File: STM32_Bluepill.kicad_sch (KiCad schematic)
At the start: 18 parts

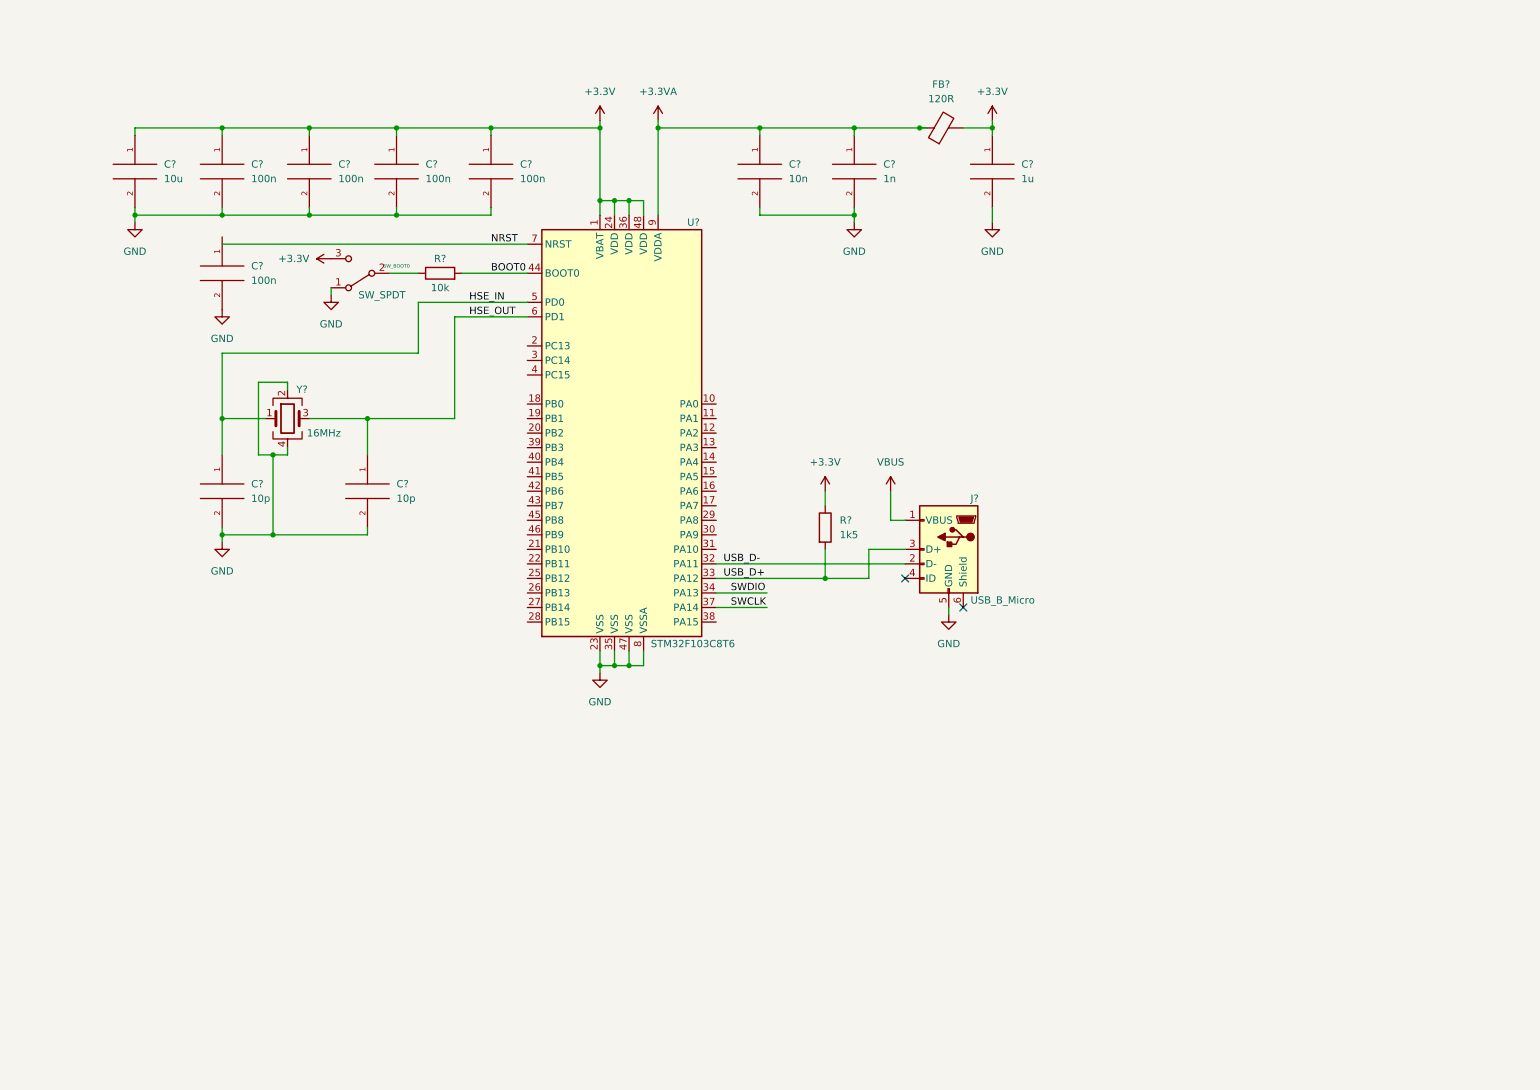
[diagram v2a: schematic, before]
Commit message: Schematic: Add power supply and connectors
	- 3.3V Linear regulator with PWR_LED
	- Connectors for USART and I2C
	- Many resistors are 1.5k to save on the BOM
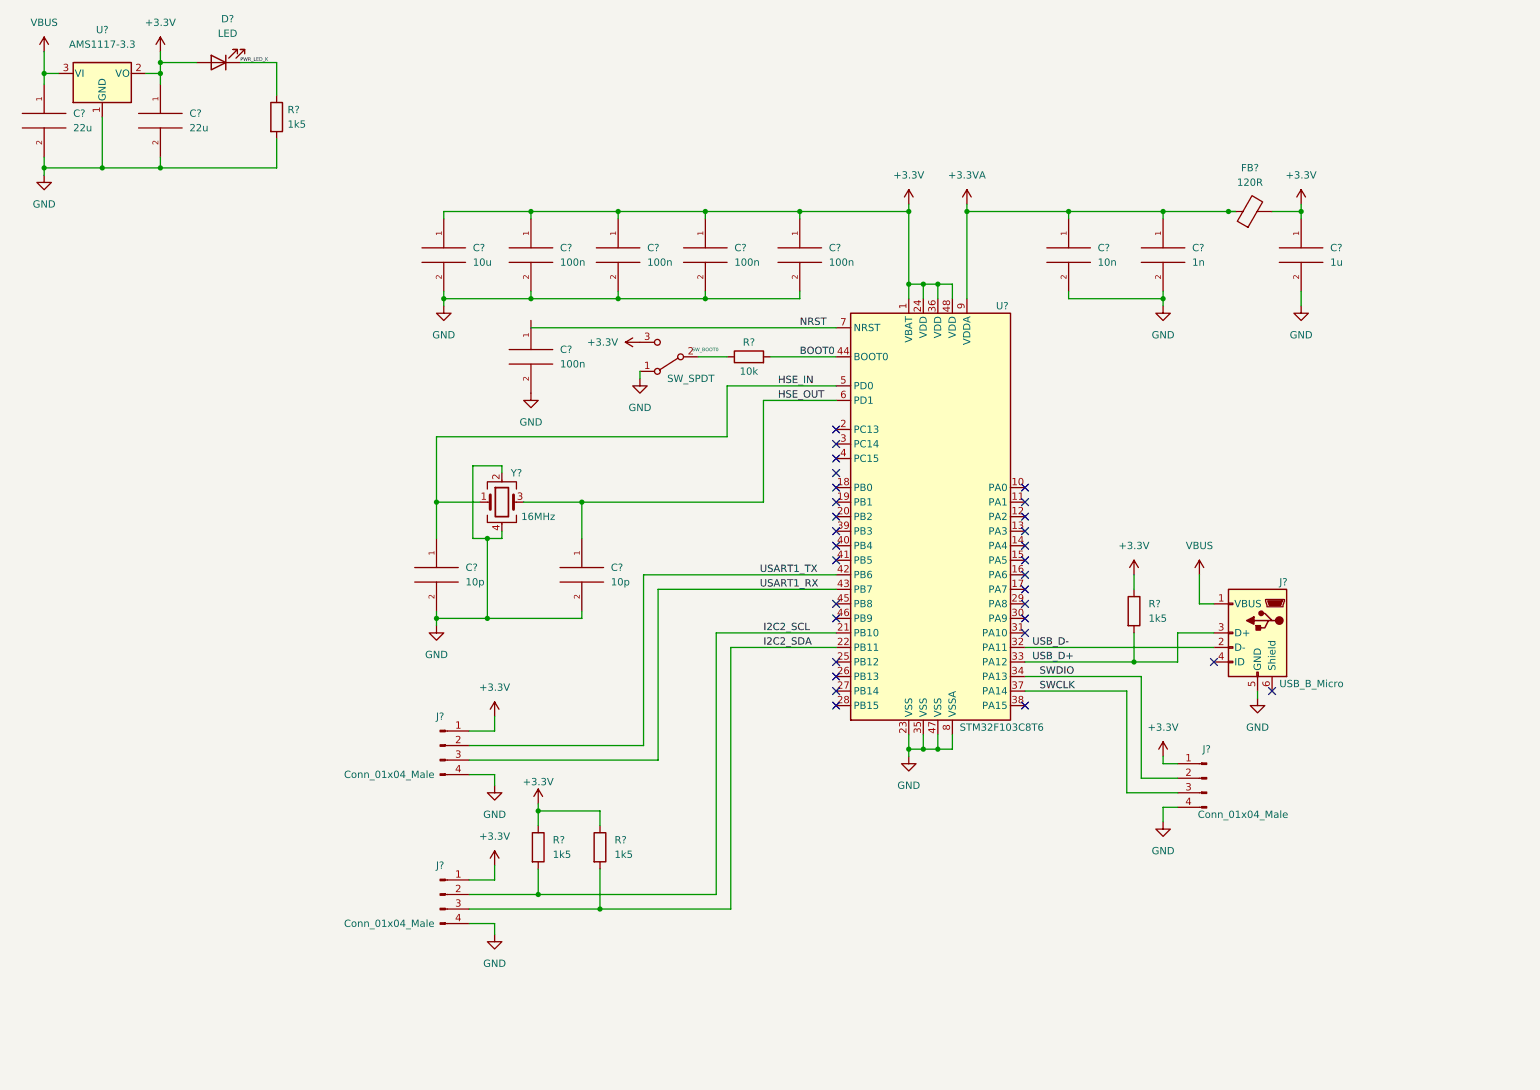
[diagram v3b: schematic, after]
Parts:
- added C? (x2): 22u, symbol pspice:C
- added D?: LED, symbol Device:LED
- added J? (x3): Conn_01x04_Male, symbol Connector:Conn_01x04_Male
- added R? (x3): 1k5, symbol Device:R
- added U?: AMS1117-3.3, Package_TO_SOT_SMD:SOT-223-3_TabPin2, symbol Regulator_Linear:AMS1117-3.3
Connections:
- net +3.3V: now also C?.1, D?.2 (A), J?.1 (Pin_1), J?.1 (Pin_1), J?.1 (Pin_1), R?.1, R?.1, U?.2 (VO)
- net GND: now also C?.2, C?.2, J?.4 (Pin_4), J?.4 (Pin_4), J?.4 (Pin_4), R?.2, U?.1 (GND)
- net SWCLK: now also J?.3 (Pin_3)
- net SWDIO: now also J?.2 (Pin_2)
- net VBUS: now also C?.1, U?.3 (VI)
- net I2C2_SCL: now reaches U?.21 (PB10)
- net I2C2_SCL: now also J?.2 (Pin_2), R?.2
- net I2C2_SDA: now reaches U?.22 (PB11)
- net I2C2_SDA: now also J?.3 (Pin_3), R?.2
- net USART1_TX: now reaches U?.42 (PB6)
- net USART1_TX: now also J?.2 (Pin_2)
- net USART1_RX: now reaches U?.43 (PB7)
- net USART1_RX: now also J?.3 (Pin_3)
- new net PWR_LED_K: D?.1 (K), R?.1
- no-connect marks 2 -> 30
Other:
- moved on the sheet: C?, FB?, J?, R?, SW_BOOT0, U?, Y?

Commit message: Schematic: Annotate and add notes and run ERC; also add PWR_FLAG
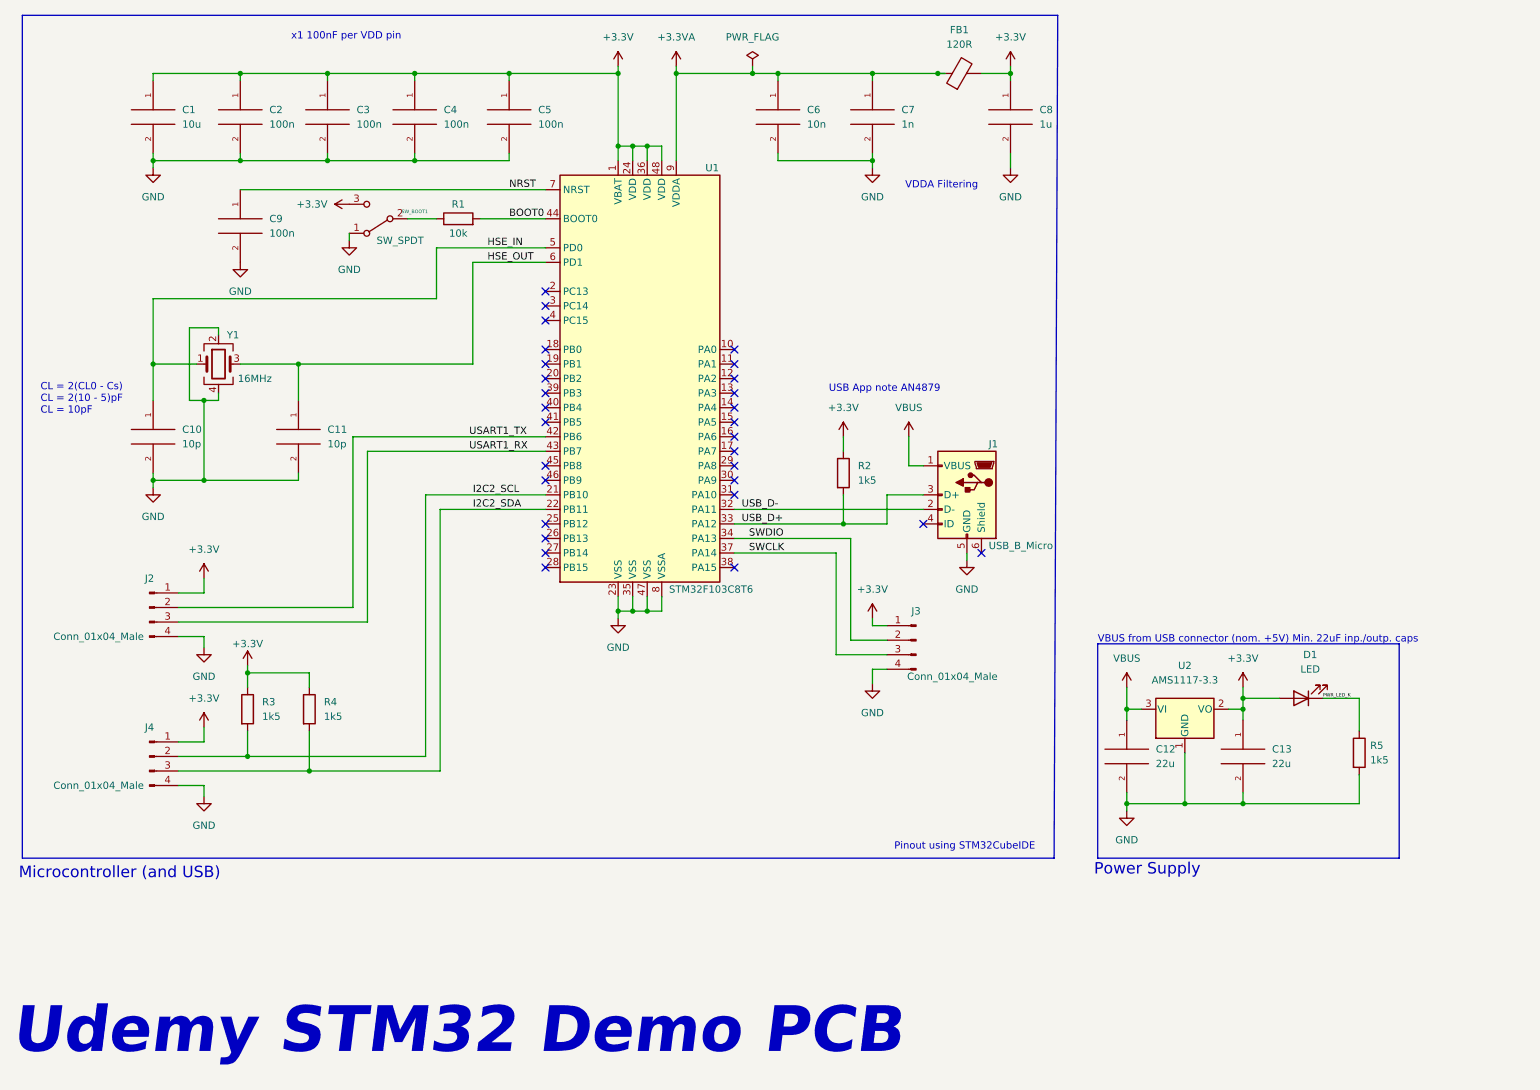
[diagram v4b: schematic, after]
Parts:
- gave numbers to parts that had none: 27
- renumbered SW_BOOT0 to SW_BOOT1
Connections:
- net NRST: now also C9.1
- no-connect marks 30 -> 29
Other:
- note added: "CL = 2(CL0 - Cs) CL = 2(10 - 5)pF CL = 10pF"
- note added: "Microcontroller (and USB)"
- note added: "Pinout using STM32CubeIDE"
- note added: "Power Supply"
- note added: "USB App note AN4879"
- note added: "Udemy STM32 Demo PCB"
- note added: "VBUS from USB connector (nom. +5V) Min. 22uF inp./outp. caps"
- note added: "VDDA Filtering"
- note added: "x1 100nF per VDD pin"
- moved on the sheet: C1, C10, C11, C12, C13, C2, C3, C4, C5, C6, C7, C8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

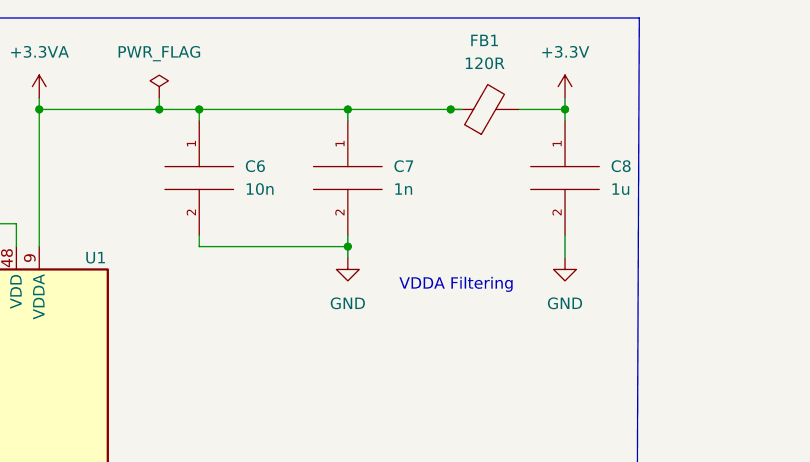
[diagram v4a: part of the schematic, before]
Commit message: Schematic: Fix wrong cap value in VDDA Filtering from 10nF to 1uF
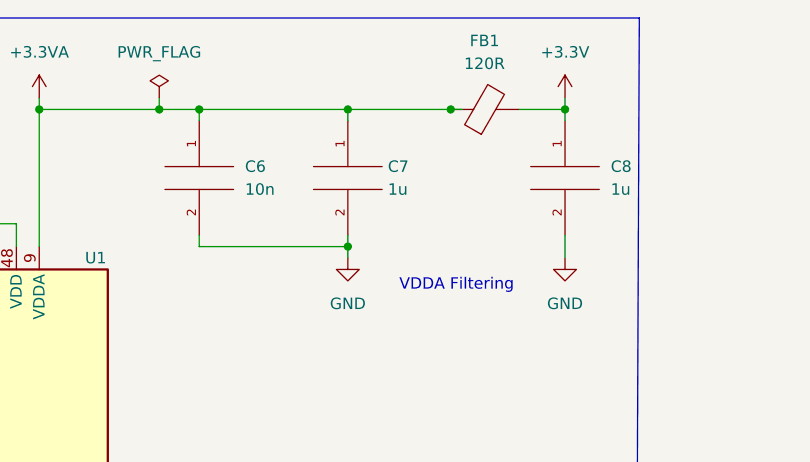
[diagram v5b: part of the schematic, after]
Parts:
- C1: footprint (none) -> Capacitor_SMD:C_0603_1608Metric
- C10, C11, C2, C3, C4, C5, C6, C8, C9: footprint (none) -> Capacitor_SMD:C_0402_1005Metric
- C12, C13: footprint (none) -> Capacitor_SMD:C_0805_2012Metric
- C7: value 1n -> 1u; footprint (none) -> Capacitor_SMD:C_0402_1005Metric
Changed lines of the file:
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@@
       (effects (font (size 1.27 1.27)) (justify left))
     )
-    (property "Footprint" "" (id 2) (at 99.695 32.385 0)
+    (property "Footprint" "Capacitor_SMD:C_0402_1005Metric" (id 2) (at 99.695 32.385 0)
       (effects (font (size 1.27 1.27)) hide)
     )
@@
       (effects (font (size 1.27 1.27)) (justify left))
     )
-    (property "Footprint" "" (id 2) (at 207.645 144.145 0)
+    (property "Footprint" "Capacitor_SMD:C_0805_2012Metric" (id 2) (at 207.645 144.145 0)
       (effects (font (size 1.27 1.27)) hide)
     )
@@
       (effects (font (size 1.27 1.27)) (justify left))
     )
-    (property "Footprint" "" (id 2) (at 146.685 32.385 0)
+    (property "Footprint" "Capacitor_SMD:C_0402_1005Metric" (id 2) (at 146.685 32.385 0)
       (effects (font (size 1.27 1.27)) hide)
     )
@@
       (effects (font (size 1.27 1.27)) (justify left))
     )
-    (property "Footprint" "" (id 2) (at 83.185 32.385 0)
+    (property "Footprint" "Capacitor_SMD:C_0402_1005Metric" (id 2) (at 83.185 32.385 0)
       (effects (font (size 1.27 1.27)) hide)
     )
@@
       (effects (font (size 1.27 1.27)) (justify left))
     )
-    (property "Footprint" "" (id 2) (at 37.465 32.385 0)
+    (property "Footprint" "Capacitor_SMD:C_0603_1608Metric" (id 2) (at 37.465 32.385 0)
       (effects (font (size 1.27 1.27)) hide)
     )
@@
       (effects (font (size 1.27 1.27)) (justify left))
     )
-    (property "Footprint" "" (id 2) (at 52.705 51.435 0)
+    (property "Footprint" "Capacitor_SMD:C_0402_1005Metric" (id 2) (at 52.705 51.435 0)
       (effects (font (size 1.27 1.27)) hide)
     )
@@
       (effects (font (size 1.27 1.27)) (justify left))
     )
-    (property "Footprint" "" (id 2) (at 187.325 32.385 0)
+    (property "Footprint" "Capacitor_SMD:C_0402_1005Metric" (id 2) (at 187.325 32.385 0)
       (effects (font (size 1.27 1.27)) hide)
     )
@@
       (effects (font (size 1.27 1.27)) (justify left))
     )
-    (property "Footprint" "" (id 2) (at 62.865 88.265 0)
+    (property "Footprint" "Capacitor_SMD:C_0402_1005Metric" (id 2) (at 62.865 88.265 0)
       (effects (font (size 1.27 1.27)) hide)
     )
@@
       (effects (font (size 1.27 1.27)) (justify left))
     )
-    (property "Footprint" "" (id 2) (at 52.705 32.385 0)
+    (property "Footprint" "Capacitor_SMD:C_0402_1005Metric" (id 2) (at 52.705 32.385 0)
       (effects (font (size 1.27 1.27)) hide)
     )
@@
   (symbol (lib_id "pspice:C") (at 163.195 32.385 0) (unit 1)
     (in_bom yes) (on_board yes) (fields_autoplaced)
-    (property "Reference" "C7" (id 0) (at 168.275 31.1149 0)
-      (effects (font (size 1.27 1.27)) (justify left))
-    )
-    (property "Value" "1n" (id 1) (at 168.275 33.6549 0)
-      (effects (font (size 1.27 1.27)) (justify left))
-    )
-    (property "Footprint" "" (id 2) (at 163.195 32.385 0)
+    (property "Reference" "C7" (id 0) (at 167.64 31.1149 0)
+      (effects (font (size 1.27 1.27)) (justify left))
+    )
+    (property "Value" "1u" (id 1) (at 167.64 33.6549 0)
+      (effects (font (size 1.27 1.27)) (justify left))
+    )
+    (property "Footprint" "Capacitor_SMD:C_0402_1005Metric" (id 2) (at 163.195 32.385 0)
       (effects (font (size 1.27 1.27)) hide)
     )
@@
       (effects (font (size 1.27 1.27)) (justify left))
     )
-    (property "Footprint" "" (id 2) (at 37.465 88.265 0)
+    (property "Footprint" "Capacitor_SMD:C_0402_1005Metric" (id 2) (at 37.465 88.265 0)
       (effects (font (size 1.27 1.27)) hide)
     )
@@
       (effects (font (size 1.27 1.27)) (justify left))
     )
-    (property "Footprint" "" (id 2) (at 227.965 144.145 0)
+    (property "Footprint" "Capacitor_SMD:C_0805_2012Metric" (id 2) (at 227.965 144.145 0)
       (effects (font (size 1.27 1.27)) hide)
     )
@@
       (effects (font (size 1.27 1.27)) (justify left))
     )
-    (property "Footprint" "" (id 2) (at 67.945 32.385 0)
+    (property "Footprint" "Capacitor_SMD:C_0402_1005Metric" (id 2) (at 67.945 32.385 0)
       (effects (font (size 1.27 1.27)) hide)
     )
@@
     )
     (path "/7442919e-faea-4635-aa80-4a1f90de056a"
-      (reference "C1") (unit 1) (value "10u") (footprint "")
+      (reference "C1") (unit 1) (value "10u") (footprint "Capacitor_SMD:C_0603_1608Metric")
     )
     (path "/a4740f12-08c6-4aec-b367-d8c2d48bb45d"
-      (reference "C2") (unit 1) (value "100n") (footprint "")
+      (reference "C2") (unit 1) (value "100n") (footprint "Capacitor_SMD:C_0402_1005Metric")
     )
     (path "/f3d3ae94-820c-4258-bc6b-8c8dd19c3469"
-      (reference "C3") (unit 1) (value "100n") (footprint "")
+      (reference "C3") (unit 1) (value "100n") (footprint "Capacitor_SMD:C_0402_1005Metric")
     )
     (path "/71c0f992-d174-4b87-baab-12d886717386"
-      (reference "C4") (unit 1) (value "100n") (footprint "")
+      (reference "C4") (unit 1) (value "100n") (footprint "Capacitor_SMD:C_0402_1005Metric")
     )
     (path "/13bfd3a7-b900-4828-95a3-91f062fc9234"
-      (reference "C5") (unit 1) (value "100n") (footprint "")
+      (reference "C5") (unit 1) (value "100n") (footprint "Capacitor_SMD:C_0402_1005Metric")
     )
     (path "/470570b2-842a-420d-ba26-f8d8bf087e99"
-      (reference "C6") (unit 1) (value "10n") (footprint "")
+      (reference "C6") (unit 1) (value "10n") (footprint "Capacitor_SMD:C_0402_1005Metric")
     )
     (path "/c24e49d2-9c35-420a-a36f-f57205be13ae"
-      (reference "C7") (unit 1) (value "1n") (footprint "")
+      (reference "C7") (unit 1) (value "1u") (footprint "Capacitor_SMD:C_0402_1005Metric")
     )
     (path "/93276f33-9461-43e5-9281-a4a01ba72afa"
-      (reference "C8") (unit 1) (value "1u") (footprint "")
+      (reference "C8") (unit 1) (value "1u") (footprint "Capacitor_SMD:C_0402_1005Metric")
     )
     (path "/897260be-12f2-4ce3-ab3d-8031db22f7cb"
-      (reference "C9") (unit 1) (value "100n") (footprint "")
+      (reference "C9") (unit 1) (value "100n") (footprint "Capacitor_SMD:C_0402_1005Metric")
     )
     (path "/c4c69945-b556-44b7-8279-6a88b68a2724"
-      (reference "C10") (unit 1) (value "10p") (footprint "")
+      (reference "C10") (unit 1) (value "10p") (footprint "Capacitor_SMD:C_0402_1005Metric")
     )
     (path "/9a2eb0b3-89cd-4e1a-9a4f-22dd779e9c77"
-      (reference "C11") (unit 1) (value "10p") (footprint "")
+      (reference "C11") (unit 1) (value "10p") (footprint "Capacitor_SMD:C_0402_1005Metric")
     )
     (path "/365e52a2-b402-40df-87b3-924556e1c5c7"
-      (reference "C12") (unit 1) (value "22u") (footprint "")
+      (reference "C12") (unit 1) (value "22u") (footprint "Capacitor_SMD:C_0805_2012Metric")
     )
     (path "/d414f452-25c3-404b-8bca-595d38f4e585"
-      (reference "C13") (unit 1) (value "22u") (footprint "")
+      (reference "C13") (unit 1) (value "22u") (footprint "Capacitor_SMD:C_0805_2012Metric")
     )
     (path "/fa2f15a9-5e95-4684-b4d4-03d2c4578c27"
